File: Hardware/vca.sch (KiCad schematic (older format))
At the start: 59 parts, among them Q1 MMBFJ177, Q2 MMBFJ177, Q3 MMBFJ177, Q4 MMBFJ177, U4 TL074

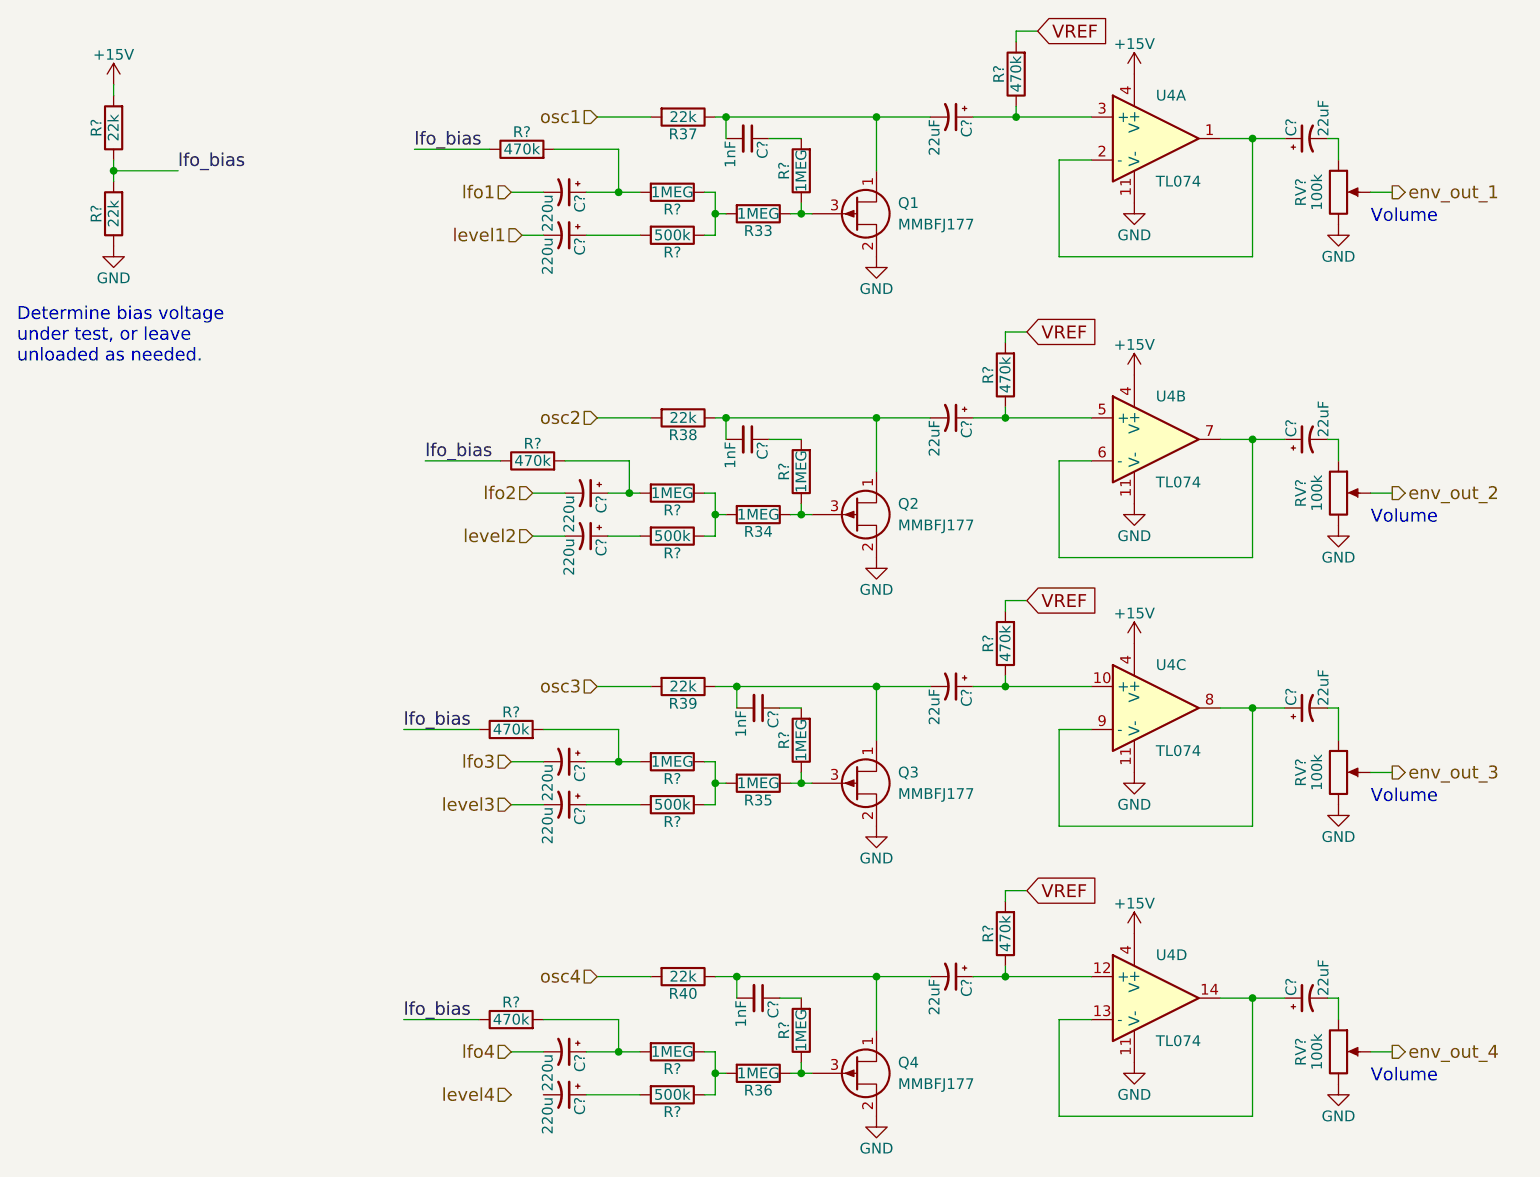
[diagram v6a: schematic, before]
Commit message: associate footprints with all components
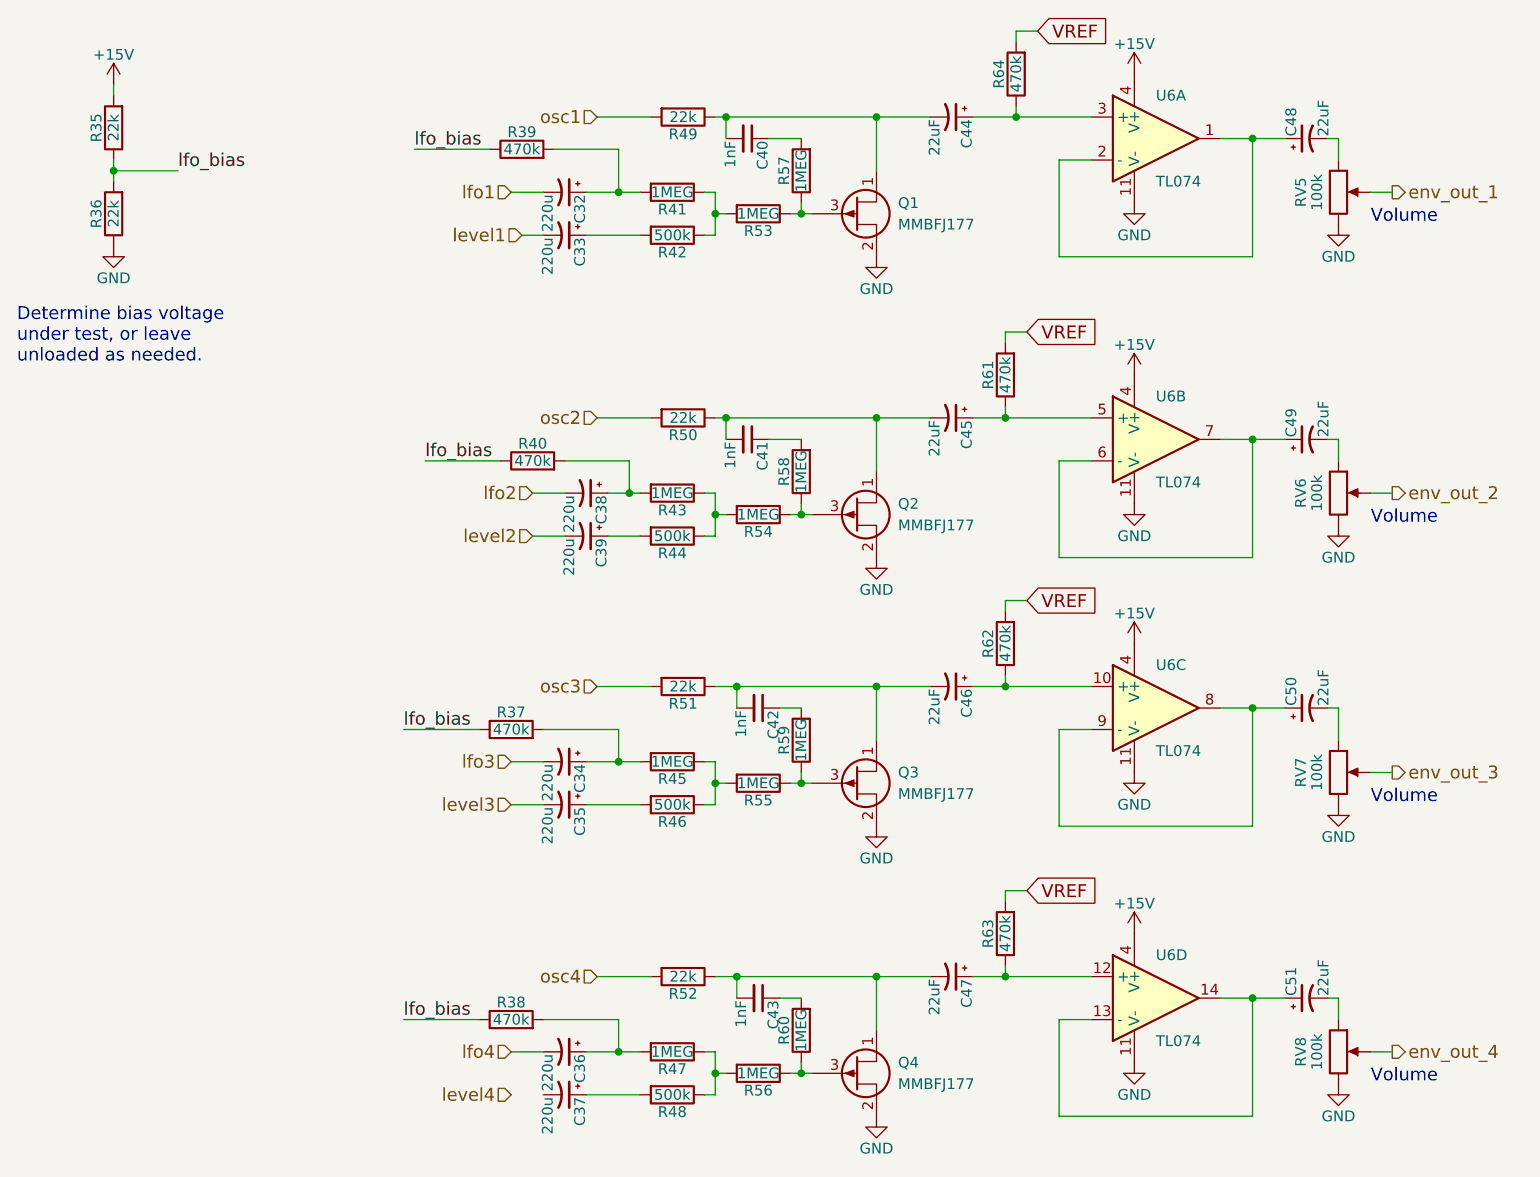
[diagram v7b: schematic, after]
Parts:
- C32, C33, C34, C35, C36, C37, C38, C39: renamed from C?; footprint (none) -> Capacitors_SMD:CP_Elec_8x10
- C40, C41, C42, C43: renamed from C?; footprint (none) -> digikey-footprints:0805
- C44, C45, C46, C47, C48, C49, C50, C51: renamed from C?; footprint (none) -> Capacitors_SMD:CP_Elec_5x5.7
- Q1, Q2, Q3, Q4: footprint (none) -> digikey-footprints:SOT-23-3
- R35, R36, R37, R38, R39, R40, R41, R42, R43, R44, R45, R46, R47, R48, R57, R58, R59, R60, R61, R62, R63, R64: renamed from R?; footprint (none) -> digikey-footprints:0805
- R49: renamed from R37; footprint (none) -> digikey-footprints:0805
- R50: renamed from R38; footprint (none) -> digikey-footprints:0805
- R51: renamed from R39; footprint (none) -> digikey-footprints:0805
- R52: renamed from R40; footprint (none) -> digikey-footprints:0805
- R53: renamed from R33; footprint (none) -> digikey-footprints:0805
- R54: renamed from R34; footprint (none) -> digikey-footprints:0805
- R55: renamed from R35; footprint (none) -> digikey-footprints:0805
- R56: renamed from R36; footprint (none) -> digikey-footprints:0805
- RV5, RV6, RV7, RV8: renamed from RV?; footprint (none) -> Potentiometers:Potentiometer_Bourns_PTV09A-1_Horizontal
- U6: renamed from U4; footprint (none) -> digikey-footprints:SOIC-14_W3.9mm

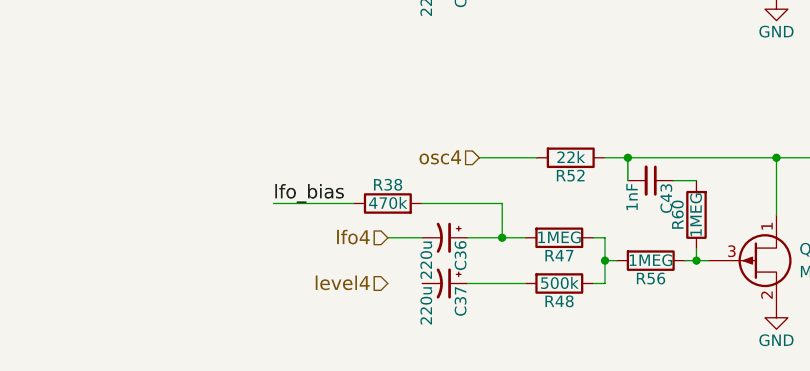
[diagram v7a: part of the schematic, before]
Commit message: complete initial PCB layout. CapSense buttons still not done, but everything else should be there. I had to increase to a 4-layer board to keep the dimensions 8"x4".
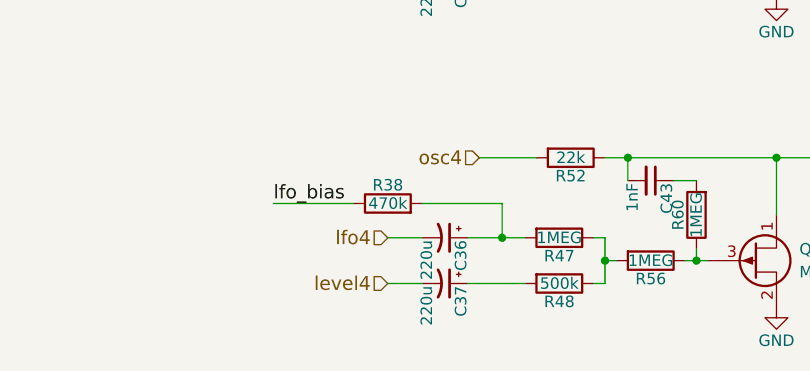
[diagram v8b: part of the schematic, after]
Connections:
- net level4: now also C37.2
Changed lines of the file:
@@
 	3750 5300 3800 5300
 Connection ~ 3800 5400
+Wire Wire Line
+	2850 5500 3000 5500
 $EndSCHEMATC
